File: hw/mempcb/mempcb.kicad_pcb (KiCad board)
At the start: 4 copper layers, 100 x 100 mm, 31 parts, among them J1 RC6502_Bus, J2 0.1" 2x25, U3 JEDEC_DIP32_RAM, U4 74LS138, U5 74LS138

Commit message: hw/mempcb: Routed pull-up/down headers
This appears to complete all routing except for Vcc and ground.
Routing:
- net Net-(PULLUP1-Pad1): track 0.00 -> 4.98 mm
- net Net-(PULLDOWN1-Pad1): track 0.00 -> 4.98 mm
- net Net-(PULLDOWN1-Pad4): track 0.00 -> 4.86 mm
- net Net-(PULLUP1-Pad4): track 0.00 -> 4.86 mm
- net Net-(PULLDOWN1-Pad3): track 0.00 -> 4.34 mm
- net Net-(PULLUP1-Pad3): track 0.00 -> 4.34 mm
- net Net-(PULLUP1-Pad2): track 0.00 -> 3.81 mm
- net Net-(PULLDOWN1-Pad2): track 0.00 -> 3.81 mm
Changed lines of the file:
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@@
     (thickness 1.6002)
     (drawings 4)
-    (tracks 458)
+    (tracks 477)
     (zones 0)
     (modules 31)
@@
   (segment (start 85.051001 54.571001) (end 87.668999 54.571001) (width 0.254) (layer Back) (net 90))
   (segment (start 83.82 53.34) (end 85.051001 54.571001) (width 0.254) (layer Back) (net 90))
+  (segment (start 165.09 133.058) (end 167.63 135.598) (width 0.254) (layer Back) (net 91))
+  (segment (start 163.82 133.058) (end 165.09 133.058) (width 0.254) (layer Back) (net 91))
+  (segment (start 166.36 130.518) (end 167.63 131.788) (width 0.254) (layer Back) (net 92))
+  (segment (start 163.82 130.518) (end 166.36 130.518) (width 0.254) (layer Back) (net 92))
+  (segment (start 165.022081 127.978) (end 167.63 127.978) (width 0.254) (layer Back) (net 93))
+  (segment (start 163.82 127.978) (end 165.022081 127.978) (width 0.254) (layer Back) (net 93))
+  (segment (start 163.82 124.334) (end 163.82 125.438) (width 0.254) (layer Back) (net 94))
+  (segment (start 163.986 124.168) (end 163.82 124.334) (width 0.254) (layer Back) (net 94))
+  (segment (start 167.63 124.168) (end 163.986 124.168) (width 0.254) (layer Back) (net 94))
+  (segment (start 166.36 108.928) (end 167.63 108.928) (width 0.254) (layer Back) (net 95))
+  (segment (start 163.82 111.468) (end 166.36 108.928) (width 0.254) (layer Back) (net 95))
+  (segment (start 166.36 114.008) (end 167.63 112.738) (width 0.254) (layer Back) (net 96))
+  (segment (start 163.82 114.008) (end 166.36 114.008) (width 0.254) (layer Back) (net 96))
+  (segment (start 165.022081 116.548) (end 167.63 116.548) (width 0.254) (layer Back) (net 97))
+  (segment (start 163.82 116.548) (end 165.022081 116.548) (width 0.254) (layer Back) (net 97))
+  (segment (start 166.49863 120.358) (end 167.63 120.358) (width 0.254) (layer Back) (net 98))
+  (segment (start 163.986 120.358) (end 166.49863 120.358) (width 0.254) (layer Back) (net 98))
+  (segment (start 163.82 120.192) (end 163.986 120.358) (width 0.254) (layer Back) (net 98))
+  (segment (start 163.82 119.088) (end 163.82 120.192) (width 0.254) (layer Back) (net 98))
   (segment (start 144.77 61.938) (end 132.07 61.938) (width 0.254) (layer Back) (net 99))
   (segment (start 137.15 64.478) (end 132.07 64.478) (width 0.254) (layer Back) (net 100))

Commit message: WIP hw/mempcb: Started power routing; now rethinking layout
- Logic caps were moved to be closer to Vcc pins; since they have immediate
  access to ground layer, the entire length is in cap-to-Vcc.
- All chips now have power, with only two component-side traces, both
  entirely under sockets and so not affecting ground return for wire wrap.

However, we now have the issue of the power sockets and the Vcc/pullup
pins, both of which would currently require vias and top-level traces. It's
probably best just to move these.
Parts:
- moved C2 28.4 mm to (102.9, 119.5)
- moved C3 2.73 mm to (132.1, 119.4)
- moved BUSPWR_EN1 0.29 mm to (129.5, 141.0)
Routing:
- net /VCC: track 22.9 -> 145.6 mm, vias 0 -> 2
- net /BUS_VCC: track 0.00 -> 13.7 mm
- net /D4: track 107.2 -> 110.7 mm
- net /D3: track 104.8 -> 107.7 mm
- net /D5: track 110.7 -> 112.8 mm
- net /D6: track 114.3 -> 115.3 mm

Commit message: WIP hw/mempcb: Move power connectors; ARGH! DIP-32 is not aligned to grid!
Moving the power connectors up to the top edge of the board lets us hook
them with under-board traces to the DIP-32 Vcc. (Back in the other corner
there was no way to route power to them without topside traces, so clearly
they don't want to go there.)

It's kind of looking like the Vcc stuff, including the pull-ups, wants
to be concentrated at the centre of the board. We could move the right
logic socket over to allow this to happen.
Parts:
- moved PWR1 99.1 mm to (142.2, 53.3), turned to 180 degrees
- moved PWR2 74.0 mm to (105.4, 53.3), turned to 180 degrees
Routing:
- net /VCC: track 145.6 -> 183.6 mm, vias 2 -> 3
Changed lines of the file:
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@@
     (thickness 1.6002)
     (drawings 4)
-    (tracks 512)
+    (tracks 519)
     (zones 0)
     (modules 31)
@@
   )
   (module Connector_JST:JST_XH_B2B-XH-A_1x02_P2.50mm_Vertical (layer Front)
-    (at 83.81 124.168 90)
+    (at 105.37 53.34 180)
     (descr "JST XH series connector, B2B-XH-A (http://www.jst-mfg.com/product/pdf/eng/eXH.pdf), generated with kicad-footprint-generator")
     (tags "connector JST XH vertical")
-    (fp_text reference PWR2 (at 1.25 -3.55 -90) (layer F.SilkS)
-      (effects (font (size 1 1) (thickness 0.15)))
-    )
-    (fp_text value JST-XH (at 1.25 4.6 -90) (layer F.Fab)
+    (fp_text reference PWR2 (at 1.25 -3.55) (layer F.SilkS)
+      (effects (font (size 1 1) (thickness 0.15)))
+    )
+    (fp_text value JST-XH (at 1.25 4.6) (layer F.Fab)
       (effects (font (size 1 1) (thickness 0.15)))
     )
@@
     (fp_line (start -2.45 3.4) (end 4.95 3.4) (layer F.Fab) (width 0.1))
     (fp_line (start -2.45 -2.35) (end -2.45 3.4) (layer F.Fab) (width 0.1))
-    (fp_text user %R (at 1.25 2.7 -90) (layer F.Fab)
-      (effects (font (size 1 1) (thickness 0.15)))
-    )
-    (pad 2 thru_hole oval (at 2.5 0 90) (size 1.7 2) (drill 1) (layers *.Cu *.Mask)
+    (fp_text user %R (at 1.25 2.7) (layer F.Fab)
+      (effects (font (size 1 1) (thickness 0.15)))
+    )
+    (pad 2 thru_hole oval (at 2.5 0 180) (size 1.7 2) (drill 1) (layers *.Cu *.Mask)
       (net 24 /GND))
-    (pad 1 thru_hole roundrect (at 0 0 90) (size 1.7 2) (drill 1) (layers *.Cu *.Mask) (roundrect_rratio 0.147059)
+    (pad 1 thru_hole roundrect (at 0 0 180) (size 1.7 2) (drill 1) (layers *.Cu *.Mask) (roundrect_rratio 0.147059)
       (net 1 /VCC))
     (model ${KISYS3DMOD}/Connector_JST.3dshapes/JST_XH_B2B-XH-A_1x02_P2.50mm_Vertical.wrl
@@
   )
   (module Connector_JST:JST_XH_B2B-XH-A_1x02_P2.50mm_Vertical (layer Front)
-    (at 83.81 133.39711 90)
+    (at 142.24 53.34 180)
     (descr "JST XH series connector, B2B-XH-A (http://www.jst-mfg.com/product/pdf/eng/eXH.pdf), generated with kicad-footprint-generator")
     (tags "connector JST XH vertical")
-    (fp_text reference PWR1 (at 1.25 -3.55 -90) (layer F.SilkS)
-      (effects (font (size 1 1) (thickness 0.15)))
-    )
-    (fp_text value JST-XH (at 1.25 4.6 -90) (layer F.Fab)
+    (fp_text reference PWR1 (at 1.25 -3.55) (layer F.SilkS)
+      (effects (font (size 1 1) (thickness 0.15)))
+    )
+    (fp_text value JST-XH (at 1.25 4.6) (layer F.Fab)
       (effects (font (size 1 1) (thickness 0.15)))
     )
@@
     (fp_line (start -2.45 3.4) (end 4.95 3.4) (layer F.Fab) (width 0.1))
     (fp_line (start -2.45 -2.35) (end -2.45 3.4) (layer F.Fab) (width 0.1))
-    (fp_text user %R (at 1.25 2.7 -90) (layer F.Fab)
-      (effects (font (size 1 1) (thickness 0.15)))
-    )
-    (pad 2 thru_hole oval (at 2.5 0 90) (size 1.7 2) (drill 1) (layers *.Cu *.Mask)
+    (fp_text user %R (at 1.25 2.7) (layer F.Fab)
+      (effects (font (size 1 1) (thickness 0.15)))
+    )
+    (pad 2 thru_hole oval (at 2.5 0 180) (size 1.7 2) (drill 1) (layers *.Cu *.Mask)
       (net 24 /GND))
-    (pad 1 thru_hole roundrect (at 0 0 90) (size 1.7 2) (drill 1) (layers *.Cu *.Mask) (roundrect_rratio 0.147059)
+    (pad 1 thru_hole roundrect (at 0 0 180) (size 1.7 2) (drill 1) (layers *.Cu *.Mask) (roundrect_rratio 0.147059)
       (net 1 /VCC))
     (model ${KISYS3DMOD}/Connector_JST.3dshapes/JST_XH_B2B-XH-A_1x02_P2.50mm_Vertical.wrl
@@
   (via (at 125.73 96.52) (size 0.9) (drill 0.4) (layers Front Back) (net 1))
   (segment (start 131.67 59.398) (end 132.07 59.398) (width 0.254) (layer Front) (net 1))
-  (segment (start 125.73 65.338) (end 131.67 59.398) (width 0.254) (layer Front) (net 1))
-  (segment (start 125.73 96.52) (end 125.73 65.338) (width 0.254) (layer Front) (net 1))
   (segment (start 125.73 118.11) (end 125.73 96.52) (width 0.254) (layer Back) (net 1))
   (segment (start 135.88 120.65) (end 135.88 117.818) (width 0.254) (layer Back) (net 1))
@@
   (segment (start 105.4 125.72) (end 105.4 122.898) (width 0.254) (layer Front) (net 1))
   (segment (start 105.41 125.73) (end 105.4 125.72) (width 0.254) (layer Front) (net 1))
+  (segment (start 142.24 57.483) (end 142.24 53.34) (width 0.254) (layer Back) (net 1))
+  (segment (start 140.325 59.398) (end 142.24 57.483) (width 0.254) (layer Back) (net 1))
+  (via (at 125.73 66.04) (size 0.9) (drill 0.4) (layers Front Back) (net 1))
+  (segment (start 125.73 96.52) (end 125.73 66.04) (width 0.254) (layer Front) (net 1))
+  (segment (start 125.73 66.04) (end 125.73 65.338) (width 0.254) (layer Front) (net 1))
+  (segment (start 126.022 59.398) (end 125.73 59.69) (width 0.254) (layer Back) (net 1))
+  (segment (start 132.07 59.398) (end 126.022 59.398) (width 0.254) (layer Back) (net 1))
+  (segment (start 125.73 59.69) (end 125.73 53.34) (width 0.254) (layer Back) (net 1))
+  (segment (start 125.73 66.04) (end 125.73 59.69) (width 0.254) (layer Back) (net 1))
+  (segment (start 105.37 53.34) (end 125.73 53.34) (width 0.254) (layer Back) (net 1))
   (segment (start 135.88 148.298) (end 135.88 145.123) (width 0.254) (layer Back) (net 2))
   (segment (start 135.88 145.123) (end 135.88 140.98) (width 0.254) (layer Back) (net 2))
@@
   (segment (start 108.49113 93.77699) (end 108.441139 93.726999) (width 0.254) (layer Back) (net 11))
   (segment (start 102.25694 148.26606) (end 102.225 148.298) (width 0.254) (layer Back) (net 11))
-  (segment (start 102.225 97.581118) (end 102.25694 97.613058) (width 0.254) (layer Back) (net 11))
   (segment (start 144.77 94.958) (end 132.07 94.958) (width 0.254) (layer Back) (net 11))
   (segment (start 102.86 145.123) (end 102.86 148.298) (width 0.254) (layer Back) (net 11))

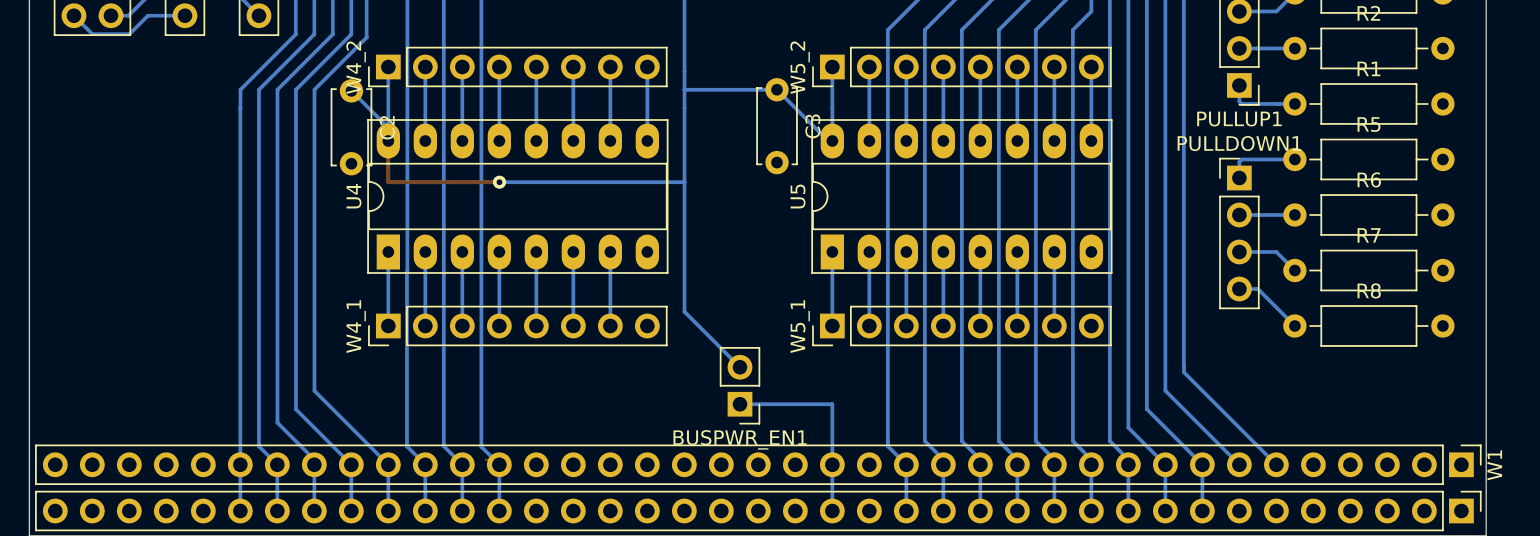
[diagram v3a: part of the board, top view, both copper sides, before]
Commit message: hw/mempcb: Move pull-downs to lower left corner
These need access only to ground, making this otherwise small empty perfect
for this. It's most likely these would be used on things related to bus
signals, anyway, so having the headers near those may work out well.
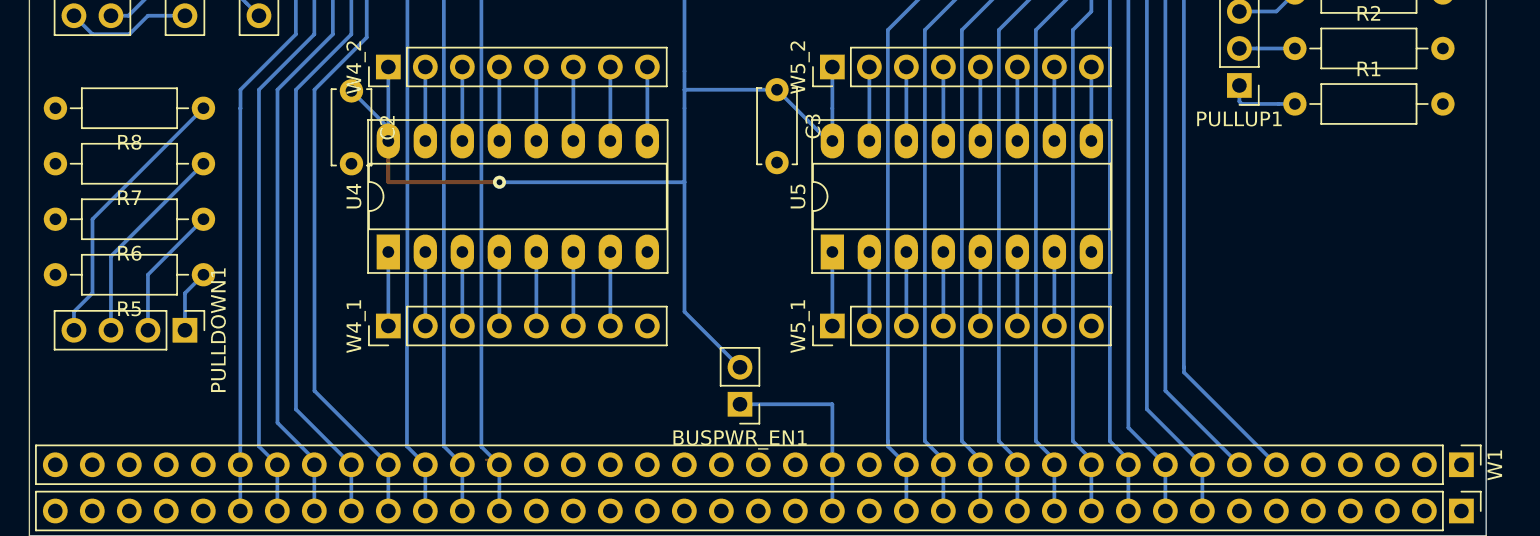
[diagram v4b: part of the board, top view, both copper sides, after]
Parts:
- moved R8 76.4 mm to (92.7, 120.7), turned to 180 degrees
- moved R5 75.3 mm to (92.7, 132.1), turned to 180 degrees
- moved R7 75.3 mm to (92.7, 124.5), turned to 180 degrees
- moved R6 74.9 mm to (92.7, 128.3), turned to 180 degrees
- moved PULLDOWN1 73.1 mm to (91.4, 135.9), turned to 270 degrees
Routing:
- net Net-(PULLDOWN1-Pad4): track 4.86 -> 18.9 mm
- net Net-(PULLDOWN1-Pad3): track 4.34 -> 14.1 mm
- net Net-(PULLDOWN1-Pad2): track 3.81 -> 9.20 mm
- net Net-(PULLDOWN1-Pad1): track 4.98 -> 4.34 mm

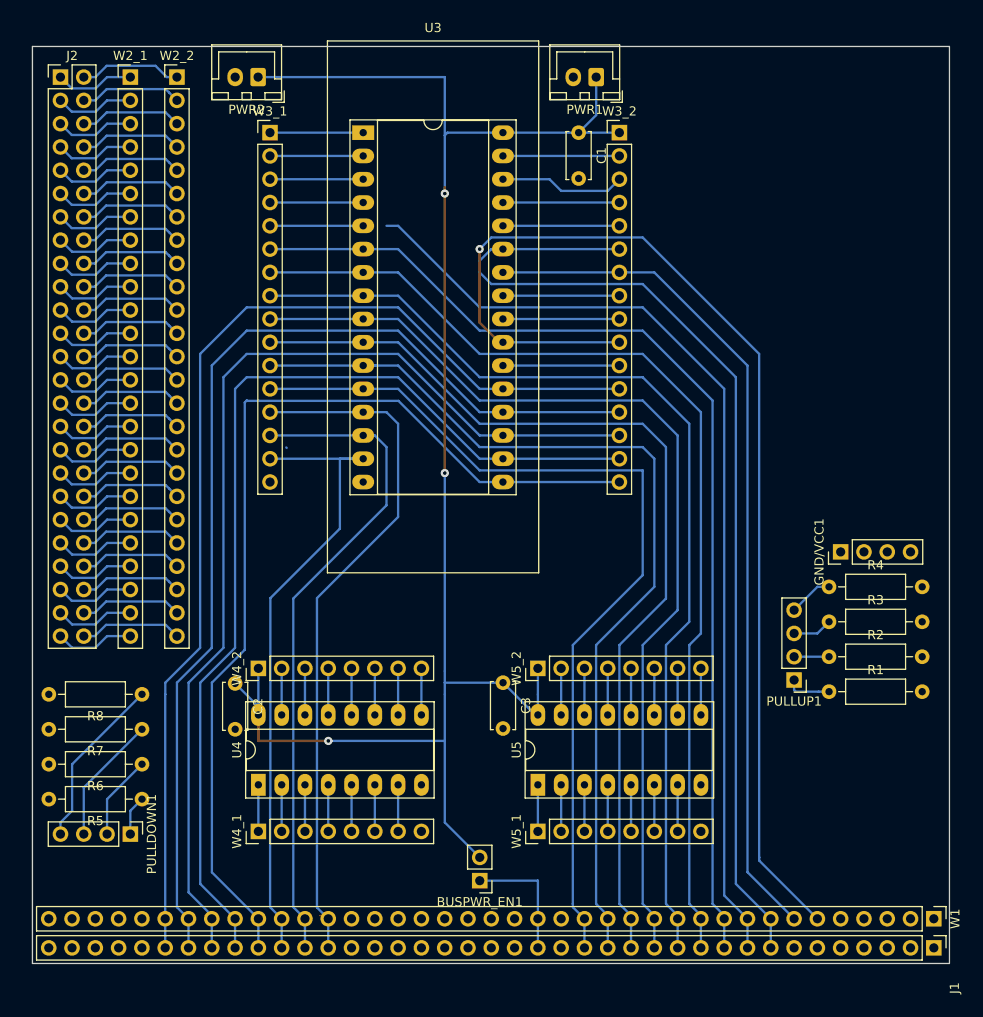
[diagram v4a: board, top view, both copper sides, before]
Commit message: hw/mempcb: Moved right logic socket to far right of board
This appears to have worked out well. The pull-ups and extra Vcc/GND pins
are in now in the centre, between the logic sockets, but not in their final
places because as it turns out I want to change around how the Vcc/GND pins
are set up, splitting them on to two separate headers. (We probably should
have done that in the first place, since a pair of headers can be placed
adjacent on the board to make what becomes one longer header.
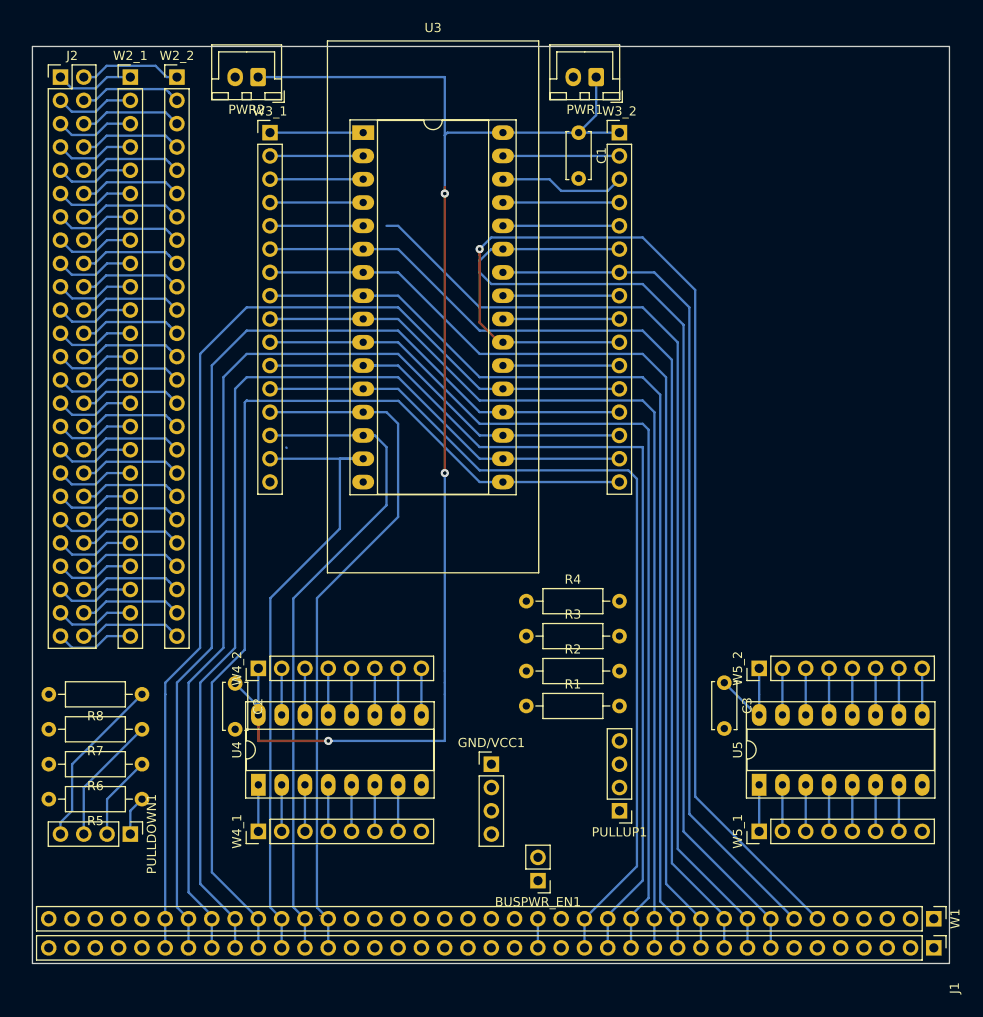
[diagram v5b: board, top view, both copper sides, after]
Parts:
- moved GND/VCC1 44.6 mm to (130.8, 128.3), turned to 0 degrees
- moved R1 33.0 mm to (134.6, 121.9)
- moved R2 33.0 mm to (134.6, 118.1)
- moved R3 33.0 mm to (134.6, 114.3)
- moved R4 33.0 mm to (134.6, 110.5)
- moved C3 24.1 mm to (156.2, 119.4)
- moved U5 24.1 mm to (160.0, 130.5)
- moved W5_1 24.1 mm to (160.0, 135.6)
- moved W5_2 24.1 mm to (160.0, 117.8)
- moved PULLUP1 23.8 mm to (144.8, 133.3)
- moved BUSPWR_EN1 6.35 mm to (135.9, 141.0)
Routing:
- net /VCC: track 183.6 -> 162.9 mm
- net /BUS_VCC: track 13.7 -> 3.18 mm
- net Net-(PULLUP1-Pad1): track 4.98 -> 0.00 mm
- net Net-(PULLUP1-Pad4): track 4.86 -> 0.00 mm
- net Net-(PULLUP1-Pad3): track 4.34 -> 0.00 mm
- net Net-(PULLUP1-Pad2): track 3.81 -> 0.00 mm
- net /A3: track 107.7 -> 104.5 mm
- net /A2: track 105.2 -> 102.5 mm
- net /A0: track 100.1 -> 97.6 mm
- net /A4: track 110.2 -> 108.1 mm
- net /A1: track 104.1 -> 102.0 mm
- net /A5: track 112.8 -> 111.7 mm
